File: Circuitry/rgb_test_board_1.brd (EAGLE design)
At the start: 31.7 x 28.4 mm, 13 parts, among them IC1 74HC595D

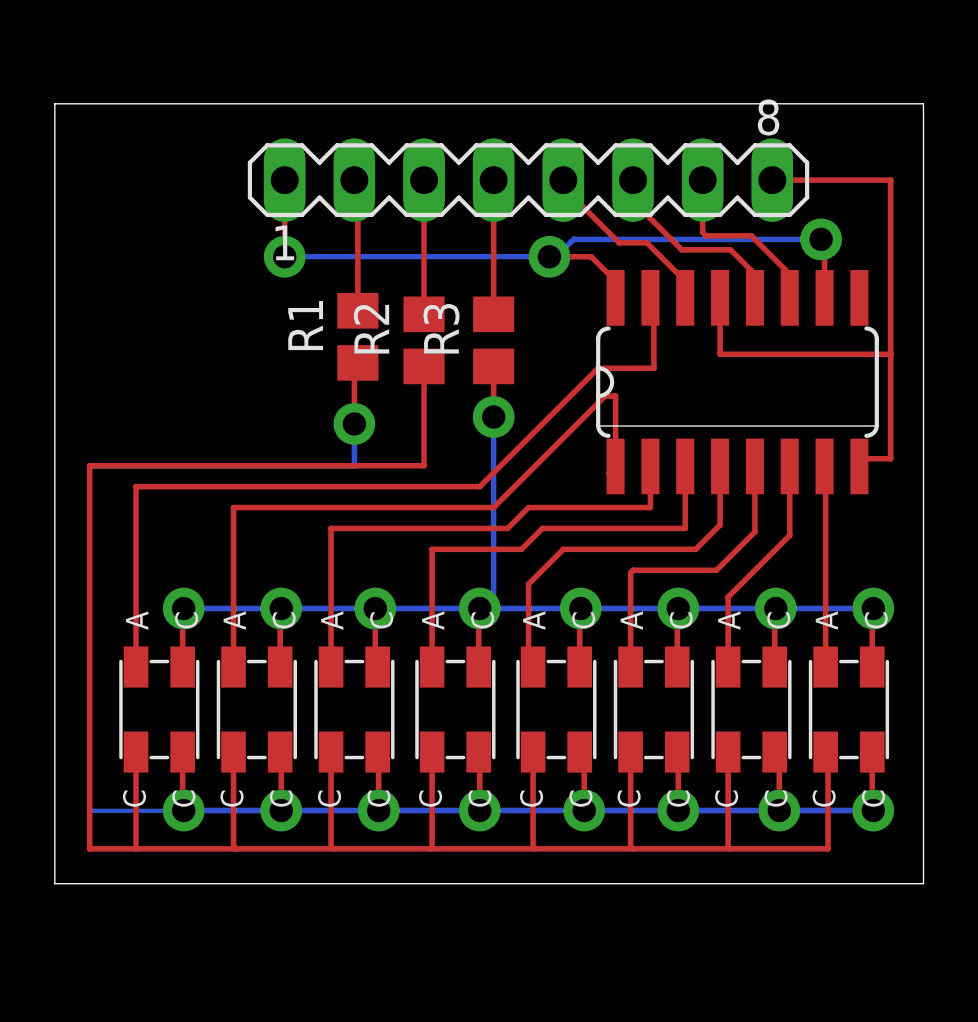
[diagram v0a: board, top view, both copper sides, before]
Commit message: create second rgb prototype
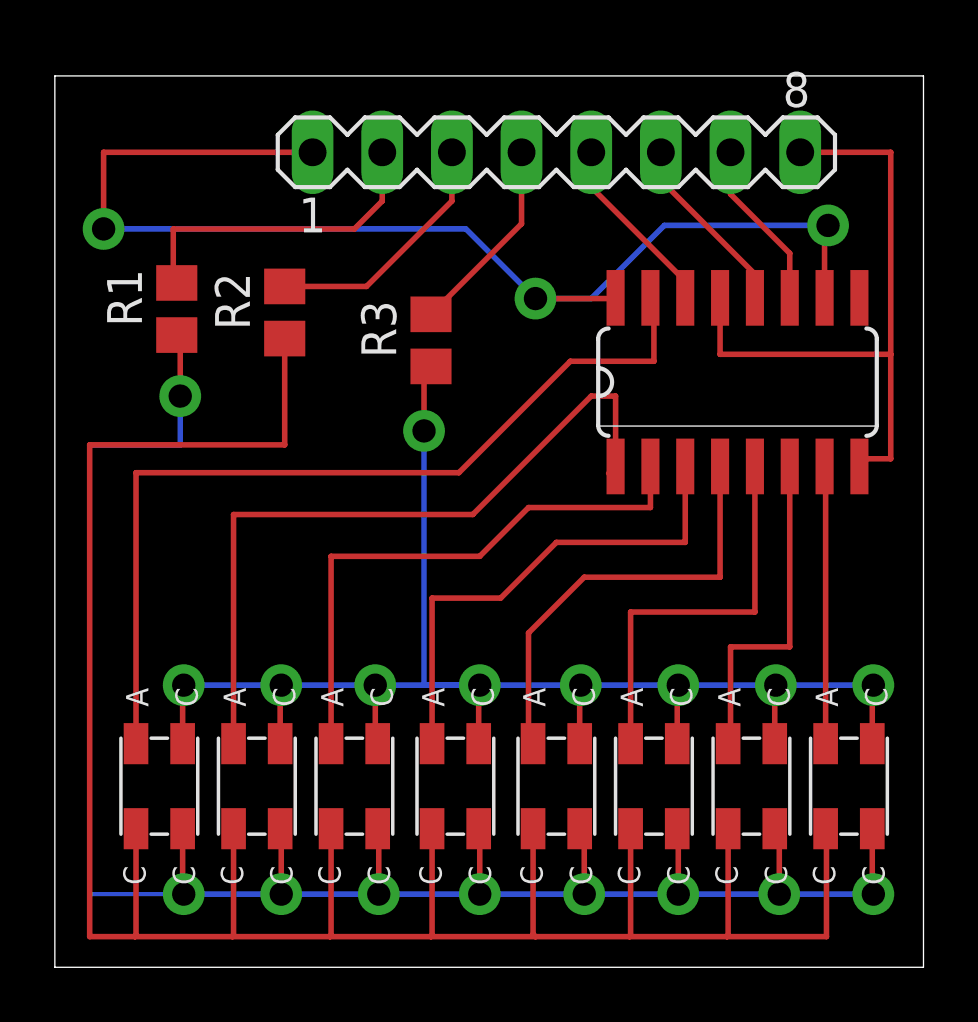
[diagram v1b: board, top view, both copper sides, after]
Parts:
- moved R1 6.68 mm to (30.9, 44.3)
- moved R2 5.18 mm to (34.8, 44.2)
- moved D1 2.79 mm to (37.3, 26.9)
- moved D2 2.79 mm to (44.7, 26.9)
- moved D3 2.79 mm to (33.8, 26.9)
- moved D4 2.79 mm to (48.3, 26.9)
- moved D5 2.79 mm to (41.0, 26.9)
- moved D6 2.79 mm to (30.2, 26.9)
- moved D7 2.79 mm to (51.8, 26.9)
- moved D8 2.79 mm to (55.4, 26.9)
- moved R3 2.29 mm to (40.1, 43.2)
- moved SV1 1.44 mm to (44.7, 50.0)
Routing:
- net VCC: track 28.4 -> 44.9 mm
- net N$1: track 4.82 -> 11.8 mm
- net N$13: track 51.2 -> 56.1 mm
- net N$2: track 4.89 -> 9.16 mm
- net N$15: track 8.25 -> 12.3 mm
- net N$8: track 11.0 -> 14.6 mm
- net N$14: track 29.9 -> 32.8 mm
- net N$7: track 13.1 -> 16.0 mm
- net N$10: track 7.33 -> 10.1 mm
- net N$4: track 24.4 -> 27.0 mm
- net N$3: track 4.89 -> 7.28 mm
- net N$16: track 85.3 -> 87.6 mm
- net N$5: track 18.5 -> 20.7 mm
- net N$6: track 16.2 -> 18.2 mm
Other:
- board size 31.7 x 28.4 mm -> 31.7 x 32.5 mm
